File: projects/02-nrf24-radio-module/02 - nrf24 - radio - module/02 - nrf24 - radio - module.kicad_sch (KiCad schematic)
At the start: 5 parts, among them J1 SPI CONNECTOR, U1 nRF24L01P

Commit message: Developing nrf24 board
Simulation of antenna matching and microstrip is started
Added monitor pins for signals to be measured
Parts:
- added J2: MONITOR_Header, Connector_PinHeader_2.54mm:PinHeader_1x06_P2.54mm_Vertical, symbol Connector:Conn_01x06_Pin
- added R2: 22K, Resistor_SMD:R_0402_1005Metric, symbol Device:R
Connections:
- net CSN: now also J2.4 (Pin_4)
- net GND: now also U1.14 (VSS), U1.17 (VSS), U1.20 (VSS), U1.8 (VSS), R2.2
- net MISO: now also J2.3 (Pin_3)
- net MOSI: now also J2.2 (Pin_2)
- net SCK: now also J2.1 (Pin_1)
- net CE: now reaches U1.1 (CE)
- net CE: now also J2.5 (Pin_5)
- net at U1.16 (IREF): now also R2.1
- net IRQ: now reaches U1.6 (IRQ)
- net IRQ: now also J2.6 (Pin_6)
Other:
- moved on the sheet: C3

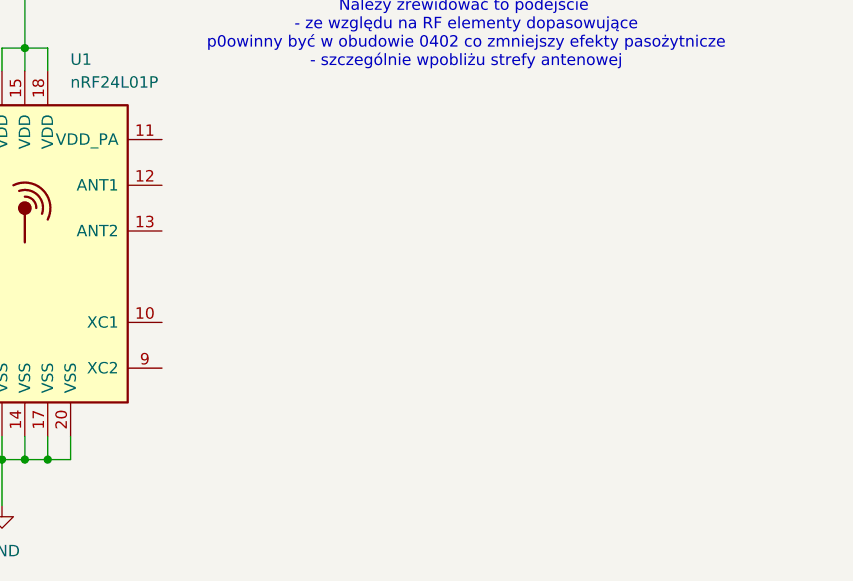
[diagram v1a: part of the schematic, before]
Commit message: +Antenna, quartz oscilator
+Chosen design idea for antenna - texas instruments inverted F antenna
+added quartz oscilator, and load capacitors
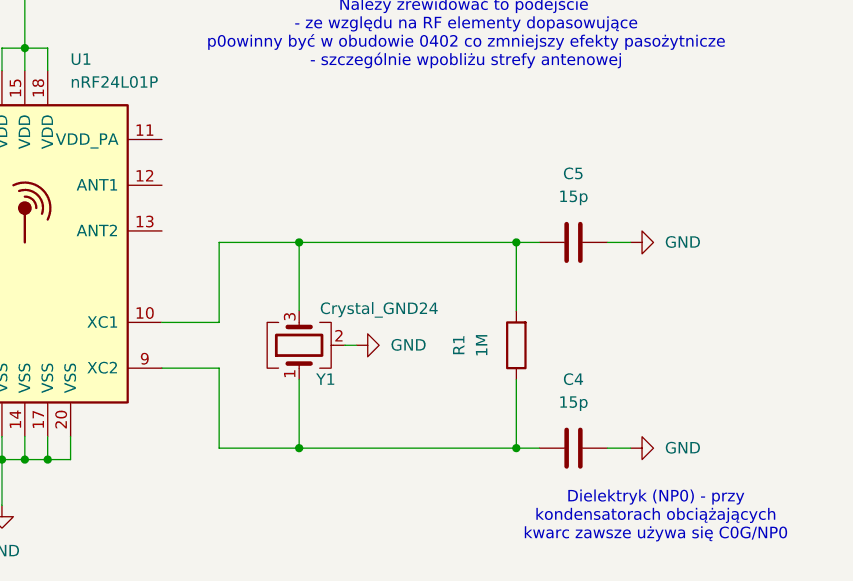
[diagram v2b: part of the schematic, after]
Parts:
- added C4, C5: 15p, Capacitor_SMD:C_0402_1005Metric, symbol Device:C
- added R1: 1M, Resistor_SMD:R_0402_1005Metric, symbol Device:R
- added Y1: Crystal_GND24, Crystal:Crystal_SMD_3225-4Pin_3.2x2.5mm, symbol Device:Crystal_GND24
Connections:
- net GND: now also C4.2, C5.2, Y1.2 (G), Y1.4 (G)
- net at U1.10 (XC1): now also C5.1, R1.2, Y1.3
- net at U1.9 (XC2): now also C4.1, R1.1, Y1.1
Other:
- note added: "Dielektryk (NP0) - przy kondensatorach obciążających kwarc zawsze używa się C0G/NP0"
